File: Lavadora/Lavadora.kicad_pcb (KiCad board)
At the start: 2 copper layers, 37 parts, among them CN1 FanPinHeader_1x03_P2.54mm_Ver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, Q01 TSOT-23, U01 DIP-8_W7.62mm_LongPads

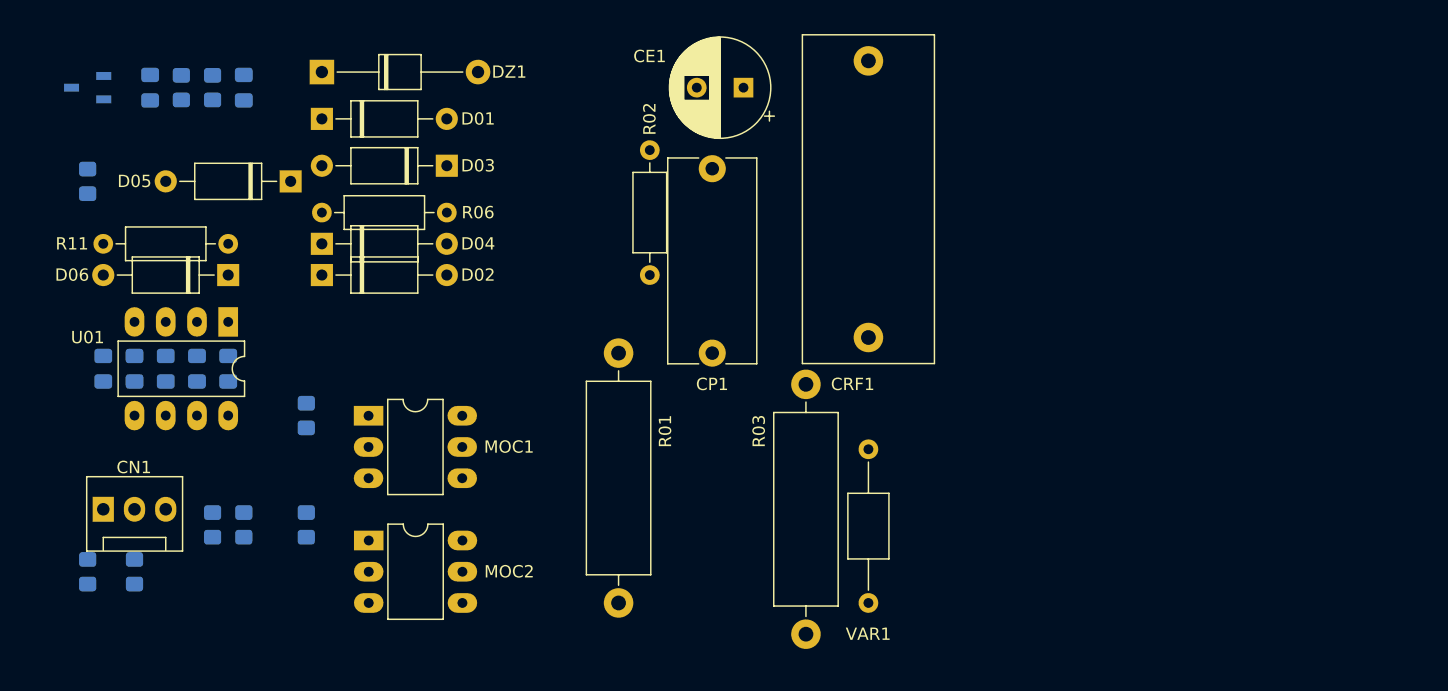
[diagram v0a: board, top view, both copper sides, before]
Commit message: Agregado componentes y pistas, exportar gerber
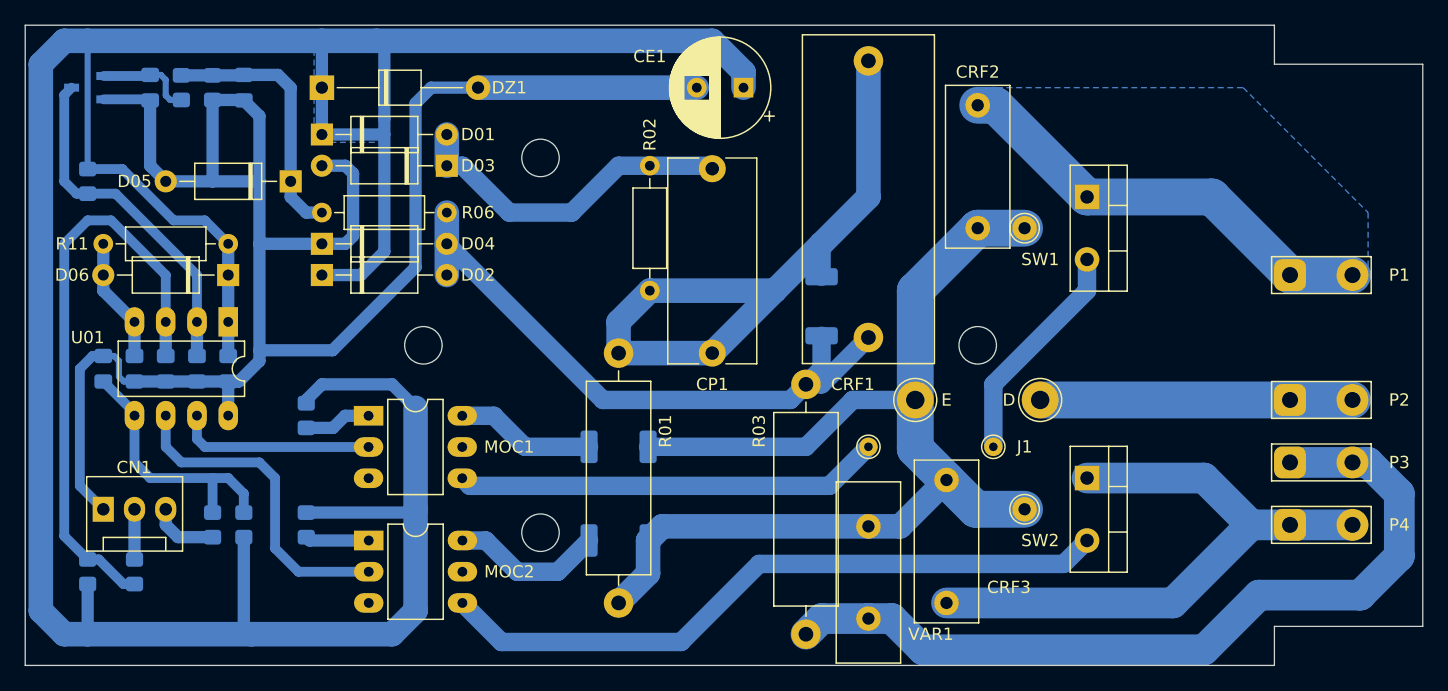
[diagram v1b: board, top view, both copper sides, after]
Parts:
- added CRF2: C_Rect_L13.0mm_W5.0mm_P10.00mm_FKS3_FKP3_MKS4, Capacitor_THT:C_Rect_L13.0mm_W5.0mm_P10.00mm_FKS3_FKP3_MKS4, F.Cu at (77.5, 16.5)
- added CRF3: C_Rect_L13.0mm_W5.0mm_P10.00mm_FKS3_FKP3_MKS4, Capacitor_THT:C_Rect_L13.0mm_W5.0mm_P10.00mm_FKS3_FKP3_MKS4, F.Cu at (74.9, 47.0)
- added D: TestPoint_THTPad_D3.0mm_Drill1.5mm, TestPoint:TestPoint_THTPad_D3.0mm_Drill1.5mm, F.Cu at (82.5, 30.5)
- added E: TestPoint_THTPad_D3.0mm_Drill1.5mm, TestPoint:TestPoint_THTPad_D3.0mm_Drill1.5mm, F.Cu at (72.4, 30.5)
- added P1: TestPoint_2Pads_Pitch5.08mm_Drill1.3mm, TestPoint:TestPoint_2Pads_Pitch5.08mm_Drill1.3mm, F.Cu at (102.9, 20.3)
- added P2: TestPoint_2Pads_Pitch5.08mm_Drill1.3mm, TestPoint:TestPoint_2Pads_Pitch5.08mm_Drill1.3mm, F.Cu at (102.9, 30.5)
- added P3: TestPoint_2Pads_Pitch5.08mm_Drill1.3mm, TestPoint:TestPoint_2Pads_Pitch5.08mm_Drill1.3mm, F.Cu at (102.9, 35.6)
- added P4: TestPoint_2Pads_Pitch5.08mm_Drill1.3mm, TestPoint:TestPoint_2Pads_Pitch5.08mm_Drill1.3mm, F.Cu at (102.9, 40.6)
- added PAD1J1: TestPoint_THTPad_D1.5mm_Drill0.7mm, TestPoint:TestPoint_THTPad_D1.5mm_Drill0.7mm, F.Cu at (78.7, 34.3)
- added PAD2J1: TestPoint_THTPad_D1.5mm_Drill0.7mm, TestPoint:TestPoint_THTPad_D1.5mm_Drill0.7mm, F.Cu at (68.6, 34.3)
- added PADSW2: TestPoint_THTPad_D2.0mm_Drill1.0mm, TestPoint:TestPoint_THTPad_D2.0mm_Drill1.0mm, F.Cu at (81.3, 39.4)
- added PADSW2: TestPoint_THTPad_D2.0mm_Drill1.0mm, TestPoint:TestPoint_THTPad_D2.0mm_Drill1.0mm, F.Cu at (81.3, 16.5)
- added R04: R_2010_5025Metric_Pad1.40x2.65mm_HandSolder, Resistor_SMD:R_2010_5025Metric_Pad1.40x2.65mm_HandSolder, B.Cu at (64.8, 22.9)
- added R08: R_2010_5025Metric_Pad1.40x2.65mm_HandSolder, Resistor_SMD:R_2010_5025Metric_Pad1.40x2.65mm_HandSolder, B.Cu at (48.3, 34.3)
- added R13: R_2010_5025Metric_Pad1.40x2.65mm_HandSolder, Resistor_SMD:R_2010_5025Metric_Pad1.40x2.65mm_HandSolder, B.Cu at (48.3, 41.9)
- added SW1: TO-220-2_Vertical, Package_TO_SOT_THT:TO-220-2_Vertical, F.Cu at (86.4, 14.0)
- added SW2: TO-220-2_Vertical, Package_TO_SOT_THT:TO-220-2_Vertical, F.Cu at (86.4, 36.8)
- VAR1: value C_Axial_L5.1mm_D3.1mm_P12.50mm_Horizontal -> C_Disc_D14.5mm_W5.0mm_P7.50mm; footprint Capacitor_THT:C_Axial_L5.1mm_D3.1mm_P12.50mm_Horizontal -> Capacitor_THT:C_Disc_D14.5mm_W5.0mm_P7.50mm
- moved D01 1.27 mm to (24.1, 8.89)
- moved DZ1 1.27 mm to (24.1, 5.08)
- moved R02 1.27 mm to (50.8, 21.6)
- moved VAR1 1.27 mm to (68.6, 48.3)
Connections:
- C01 pad 1: (no net) -> ISLA1
- C01 pad 2: (no net) -> ISLA4
- C02 pad 1: (no net) -> ISLA1
- C03 pad 1: (no net) -> ISLA1
- C04 pad 2: (no net) -> ISLA1
- C05 pad 1: (no net) -> ISLA1
- C06 pad 1: (no net) -> ISLA1
- C07 pad 1: (no net) -> ISLA1
- CE1 pad 1: (no net) -> ISLA4
- CE1 pad 2: (no net) -> ISLA1
- CN1 pad 1: (no net) -> ISLA1
- CP1 pad 1: (no net) -> ISLA2
- CRF1 pad 2: (no net) -> ISLA2
- D01 pad 1: (no net) -> ISLA4
- D02 pad 1: (no net) -> ISLA4
- D03 pad 2: (no net) -> ISLA1
- D04 pad 1: (no net) -> ISLA1
- D05 pad 2: (no net) -> ISLA1
- D06 pad 1: (no net) -> ISLA4
- DZ1 pad 1: (no net) -> ISLA4
- DZ1 pad 2: (no net) -> ISLA1
- Q01 pad 2: (no net) -> ISLA1
- R01 pad 2: (no net) -> ISLA2
- R02 pad 1: (no net) -> ISLA2
- R05 pad 2: (no net) -> ISLA4
- R07 pad 2: (no net) -> ISLA4
- R10 pad 1: (no net) -> ISLA1
- R11 pad 2: (no net) -> ISLA4
- R12 pad 2: (no net) -> ISLA4
- R14 pad 1: (no net) -> ISLA4
- R15 pad 1: (no net) -> ISLA4
- U01 pad 1: (no net) -> ISLA4
- U01 pad 8: (no net) -> ISLA1
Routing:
- net (no net): track 0.00 -> 646.6 mm
- net ISLA4: track 0.00 -> 254.2 mm
- net ISLA1: track 0.00 -> 149.7 mm
- net ISLA2: track 0.00 -> 55.6 mm
- net ISLA3: track 0.00 -> 36.2 mm
- added copper zone on B.Cu, net ISLA1
- added copper zone on B.Cu, net ISLA2
- added copper zone on B.Cu, net ISLA3
- added copper zone on B.Cu, net ISLA4
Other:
- board outline added: 113.7 x 52.1 mm
- board text added: "J1"
